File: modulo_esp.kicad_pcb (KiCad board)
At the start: 2 copper layers, 180 parts, among them CON1 USB_B_Micro, CON2 Barrel_Jack_MountingPin, CON3 8P8C, CON4 SIM_CARD, J1 104426-8, J2 104426-8, J3 SMA_CONNECTOR, Q1 AO3401A, Q10 BC817, Q11 BC817, Q2 BC817, Q3 BC817, Q4 BC817, Q5 BC817, Q6 BC817, Q7 BC817, Q8 BC817, Q9 BC817, SW1 SW_Push, SW2 SW_Push, SW3 SW_Push, SW4 SW_Push, U1 AP1117-33, U2 AP6503, U3 CP2102N, U4 IP101GRI, U5 ESP32-WROOM-32D, U6 BG95-M3, X1 25MHz

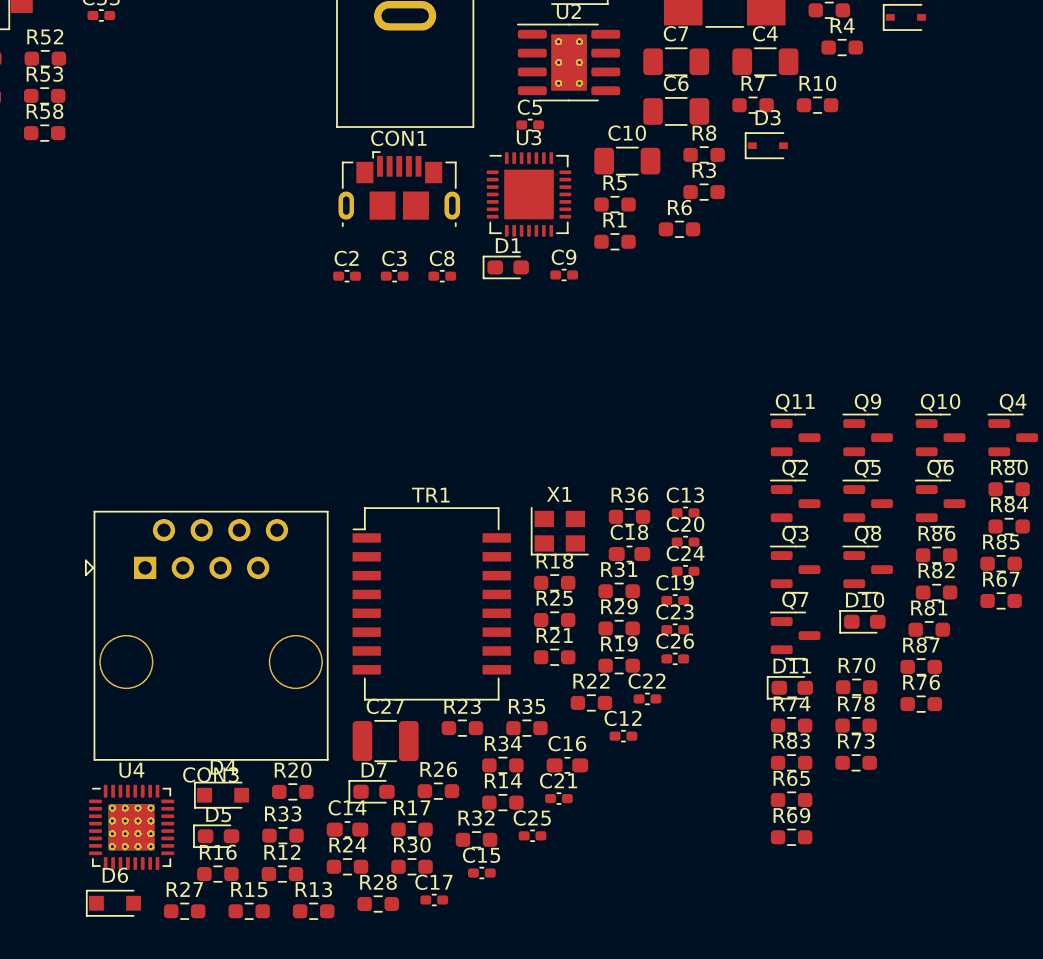
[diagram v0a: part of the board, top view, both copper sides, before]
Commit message: Inserido proteção ESD no SIM Card
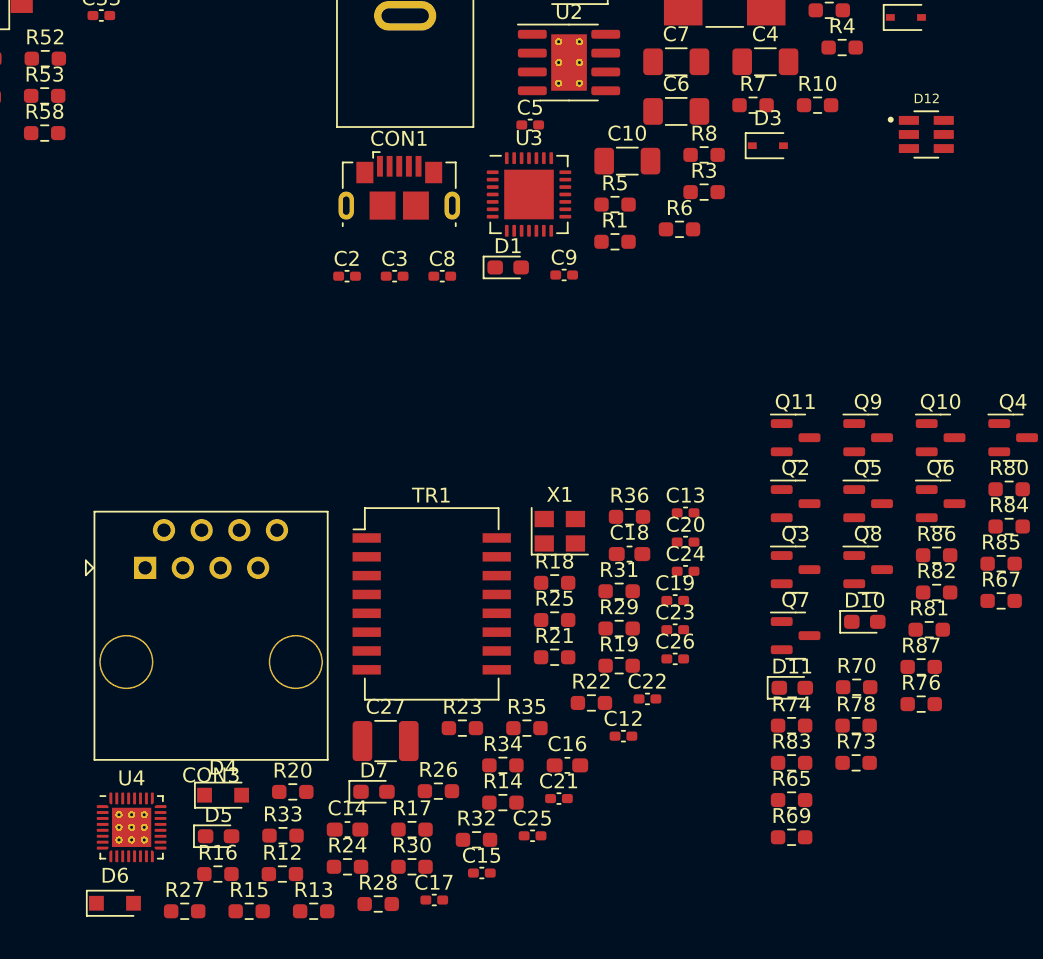
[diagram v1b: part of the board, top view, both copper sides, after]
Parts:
- added D12: ESDA6V1BC6, Alexandre_Library:ESDA6V1BC6, F.Cu at (182.8, 77.2)
- U4: footprint Package_DFN_QFN:HVQFN-32-1EP_5x5mm_P0.5mm_EP3.1x3.1mm_ThermalVias -> Package_DFN_QFN:QFN-32-1EP_4x4mm_P0.4mm_EP2.65x2.65mm_ThermalVias
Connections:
- net Net-(C45-Pad2) renamed /BG95M3/SIM_CARD/RST
- net Net-(C46-Pad2) renamed /BG95M3/SIM_CARD/CLK
- C44 pad 2: Net-(C44-Pad2) -> /BG95M3/SIM_CARD/CIO
- CON4 pad 7: GND -> /BG95M3/SIM_CARD/CIO
- R61 pad 1: Net-(C44-Pad2) -> /BG95M3/SIM_CARD/CIO
- R63 pad 2: Net-(C44-Pad2) -> /BG95M3/SIM_CARD/CIO

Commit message: Adicionado os pads dos Test Point e alterado o Bead
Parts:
- added FB1: MPZ2012S102AT000, Alexandre_Library:BEADC2012X105N, F.Cu at (162.5, 82.3)
- added FB2: MPZ2012S102AT000, Alexandre_Library:BEADC2012X105N, F.Cu at (158.1, 82.3)
- added TP1: TestPoint, TestPoint:TestPoint_Pad_1.5x1.5mm, F.Cu at (138.0, 87.9)
- added TP2: TestPoint, TestPoint:TestPoint_Pad_1.5x1.5mm, F.Cu at (149.0, 82.5)
- added TP3: TestPoint, TestPoint:TestPoint_Pad_1.5x1.5mm, F.Cu at (138.5, 82.0)
- added TP4: TestPoint, TestPoint:TestPoint_Pad_1.5x1.5mm, F.Cu at (145.5, 82.5)
- added TP5: TestPoint, TestPoint:TestPoint_Pad_1.5x1.5mm, F.Cu at (145.5, 86.1)
- C11: footprint Capacitor_SMD:C_1206_3216Metric_Pad1.33x1.80mm_HandSolder -> Capacitor_SMD:C_0603_1608Metric_Pad1.08x0.95mm_HandSolder
- C12, C13, C15, C17, C19, C2, C20, C21, C22, C23, C24, C25, C26, C29, C3, C30, C31, C32, C33, C37, C38, C39, C41, C42, C43, C44, C45, C46, C47, C5, C8, C9: footprint Capacitor_SMD:C_0402_1005Metric_Pad0.74x0.62mm_HandSolder -> Capacitor_SMD:C_0603_1608Metric_Pad1.08x0.95mm_HandSolder
- moved U5 90.6 mm to (173.8, 107.6), turned to -90 degrees
- moved R37 68.0 mm to (179.8, 96.0), turned to 180 degrees
- moved C44 67.3 mm to (150.8, 38.5)
- moved CON4 67.3 mm to (144.5, 30.2)
- moved R64 67.3 mm to (149.3, 36.3)
- moved R68 67.3 mm to (142.8, 54.7)
- moved R86 67.3 mm to (133.0, 61.1)
- moved C1 67.3 mm to (126.6, 21.4)
- moved C10 67.3 mm to (112.1, 34.5)
- moved C11 67.3 mm to (126.6, 18.1)
- moved C12 67.3 mm to (111.9, 73.3)
- moved C13 67.3 mm to (116.1, 58.3)
- moved C14 67.3 mm to (93.3, 79.6)
- moved C16 67.3 mm to (108.1, 75.3)
- moved C17 67.3 mm to (99.1, 84.4)
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- renumbered D12 to D10, D10 to D11, D11 to D12, L4 to L1
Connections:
- C1 pad 1: +3V3 -> <NO NET>
- C2 pad 2: +3V3 -> <NO NET>
- C36 pad 1: +3V3 -> <NO NET>
- C37 pad 2: +3V3 -> <NO NET>
- C38 pad 2: +3V3 -> <NO NET>
- C39 pad 2: +3V3 -> <NO NET>
- C40 pad 1: +3V3 -> <NO NET>
- C41 pad 2: +3V3 -> <NO NET>
- C42 pad 2: +3V3 -> <NO NET>
- C43 pad 2: +3V3 -> <NO NET>
- C7 pad 1: +3V3 -> <NO NET>
- R1 pad 1: +3V3 -> <NO NET>
- R5 pad 1: +3V3 -> <NO NET>
- R67 pad 2: +3V3 -> <NO NET>
- R68 pad 2: +3V3 -> <NO NET>
- R69 pad 2: +3V3 -> <NO NET>
- R70 pad 2: +3V3 -> <NO NET>
- R77 pad 2: +3V3 -> <NO NET>
- R78 pad 2: +3V3 -> <NO NET>
- R79 pad 1: +3V3 -> <NO NET>
- R80 pad 2: +3V3 -> <NO NET>
- R81 pad 1: +3V3 -> <NO NET>
- R82 pad 1: +3V3 -> <NO NET>
- R87 pad 1: +3V3 -> <NO NET>
- R88 pad 1: +3V3 -> <NO NET>
- U1 pad 2: +3V3 -> <NO NET>
- U3 pad 6: +3V3 -> <NO NET>
- U3 pad 7: +3V3 -> <NO NET>
- U6 pad 29: +3V3 -> <NO NET>
- U6 pad 32: +3V3 -> <NO NET>
- U6 pad 33: +3V3 -> <NO NET>
- U6 pad 52: +3V3 -> <NO NET>
- U6 pad 53: +3V3 -> <NO NET>

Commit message: Iniciando a posicionar os componentes no PCB
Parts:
- removed the L1 at (23.7, 99.6)
- removed L2, L3: BEAD, Inductor_SMD:L_0603_1608Metric_Pad1.05x0.95mm_HandSolder
- moved SW1 156.1 mm to (157.7, 142.6)
- moved SW2 145.5 mm to (147.3, 142.6), turned to 180 degrees
- moved SW4 138.8 mm to (147.4, 137.2), turned to 180 degrees
- moved C32 137.5 mm to (160.1, 133.9), turned to 180 degrees
- moved SW3 134.8 mm to (157.7, 137.0)
- moved C31 133.6 mm to (152.3, 133.9)
- moved R58 131.1 mm to (156.2, 133.9)
- moved C33 128.6 mm to (144.7, 133.9), turned to 180 degrees
- moved R59 126.4 mm to (148.5, 133.9)
- moved CON1 121.9 mm to (192.6, 111.6), turned to 90 degrees
- moved U1 113.2 mm to (172.2, 114.4), turned to -90 degrees
- moved CON2 112.4 mm to (184.2, 89.5), turned to 90 degrees
- moved C7 108.0 mm to (177.5, 116.2), turned to 90 degrees
- moved C2 107.4 mm to (182.0, 102.7), turned to 180 degrees
- moved C8 107.2 mm to (187.7, 103.5), turned to -90 degrees
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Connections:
- C1 pad 1: <NO NET> -> +3V3
- C10 pad 1: <NO NET> -> VCC
- C11 pad 1: <NO NET> -> VCC
- C2 pad 2: <NO NET> -> +3V3
- C36 pad 1: <NO NET> -> +3V3
- C37 pad 2: <NO NET> -> +3V3
- C38 pad 2: <NO NET> -> +3V3
- C39 pad 2: <NO NET> -> +3V3
- C4 pad 1: <NO NET> -> VCC
- C40 pad 1: <NO NET> -> +3V3
- C41 pad 2: <NO NET> -> +3V3
- C42 pad 2: <NO NET> -> +3V3
- C43 pad 2: <NO NET> -> +3V3
- C5 pad 2: <NO NET> -> VCC
- C6 pad 1: <NO NET> -> /POWER_SUPPLY/+3.9V
- C7 pad 1: <NO NET> -> +3V3
- D3 pad 1: <NO NET> -> VCC
- FB1 pad 2: <NO NET> -> +3V3
- FB2 pad 2: <NO NET> -> +3V3
- J2 pad 1: <NO NET> -> +3V3
- J2 pad 2: <NO NET> -> +3V3
- L1 pad 2: <NO NET> -> /POWER_SUPPLY/+3.9V
- Q1 pad 3: <NO NET> -> VCC
- R1 pad 1: <NO NET> -> +3V3
- R2 pad 1: <NO NET> -> VCC
- R4 pad 1: <NO NET> -> /POWER_SUPPLY/+3.9V
- R5 pad 1: <NO NET> -> +3V3
- R67 pad 2: <NO NET> -> +3V3
- R68 pad 2: <NO NET> -> +3V3
- R69 pad 2: <NO NET> -> +3V3
- R70 pad 2: <NO NET> -> +3V3
- R77 pad 2: <NO NET> -> +3V3
- R78 pad 2: <NO NET> -> +3V3
- R79 pad 1: <NO NET> -> +3V3
- R80 pad 2: <NO NET> -> +3V3
- R81 pad 1: <NO NET> -> +3V3
- R82 pad 1: <NO NET> -> +3V3
- R87 pad 1: <NO NET> -> +3V3
- R88 pad 1: <NO NET> -> +3V3
- TP1 pad 1: <NO NET> -> VCC
- TP2 pad 1: <NO NET> -> /POWER_SUPPLY/+3.9V
- TP3 pad 1: <NO NET> -> +3V3
- U1 pad 2: <NO NET> -> +3V3
- U1 pad 3: <NO NET> -> /POWER_SUPPLY/+3.9V
- U2 pad 2: <NO NET> -> VCC
- U3 pad 6: <NO NET> -> +3V3
- U3 pad 7: <NO NET> -> +3V3
- U6 pad 29: <NO NET> -> +3V3
- U6 pad 32: <NO NET> -> +3V3
- U6 pad 33: <NO NET> -> +3V3
- U6 pad 52: <NO NET> -> +3V3
- U6 pad 53: <NO NET> -> +3V3

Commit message: Continuando com o desenvolvimento do layout
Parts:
- moved C35 235.4 mm to (258.4, 142.2)
- moved C41 229.4 mm to (253.2, 151.2), turned to 180 degrees
- moved J3 225.1 mm to (259.2, 151.0), turned to 180 degrees
- moved C40 219.7 mm to (252.9, 155.2)
- moved C42 218.1 mm to (253.2, 149.5), turned to 180 degrees
- moved R60 218.0 mm to (259.2, 144.5), turned to 90 degrees
- moved C34 217.8 mm to (258.6, 146.8)
- moved U6 216.1 mm to (239.1, 143.7), turned to -90 degrees
- moved J2 212.8 mm to (242.0, 100.4)
- moved C43 212.5 mm to (253.2, 147.8), turned to 180 degrees
- moved J1 193.6 mm to (242.0, 96.5)
- moved C28 151.1 mm to (182.3, 118.1)
- moved CON3 147.9 mm to (203.6, 142.6)
- moved CON4 144.3 mm to (260.6, 116.0), turned to 180 degrees
- moved C29 143.4 mm to (182.3, 120.3)
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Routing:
- net (no net): track 0.00 -> 80.6 mm
- net /BG95M3/ANT_MAIN: track 0.00 -> 12.7 mm
- net Net-(C34-Pad2): track 0.00 -> 5.26 mm
